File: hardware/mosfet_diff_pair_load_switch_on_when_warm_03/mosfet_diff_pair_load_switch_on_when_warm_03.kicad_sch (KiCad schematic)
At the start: 18 parts, among them Q1 IRLML2402TR, Q2 IRLML2402TR

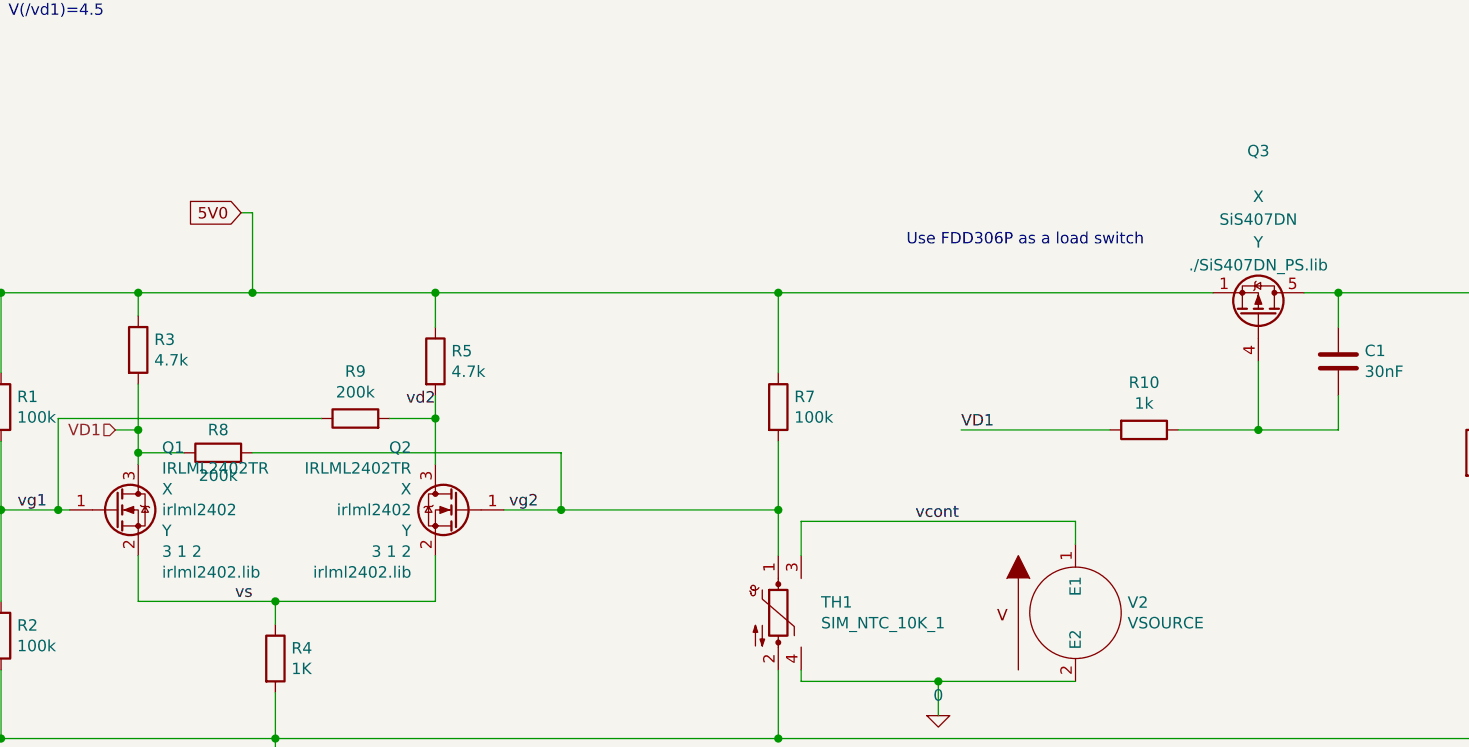
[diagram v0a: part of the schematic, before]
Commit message: Changing pass transistor from FDD306 and long-tail pair transistors from irlml2402 becuase they aren't available at the moment.
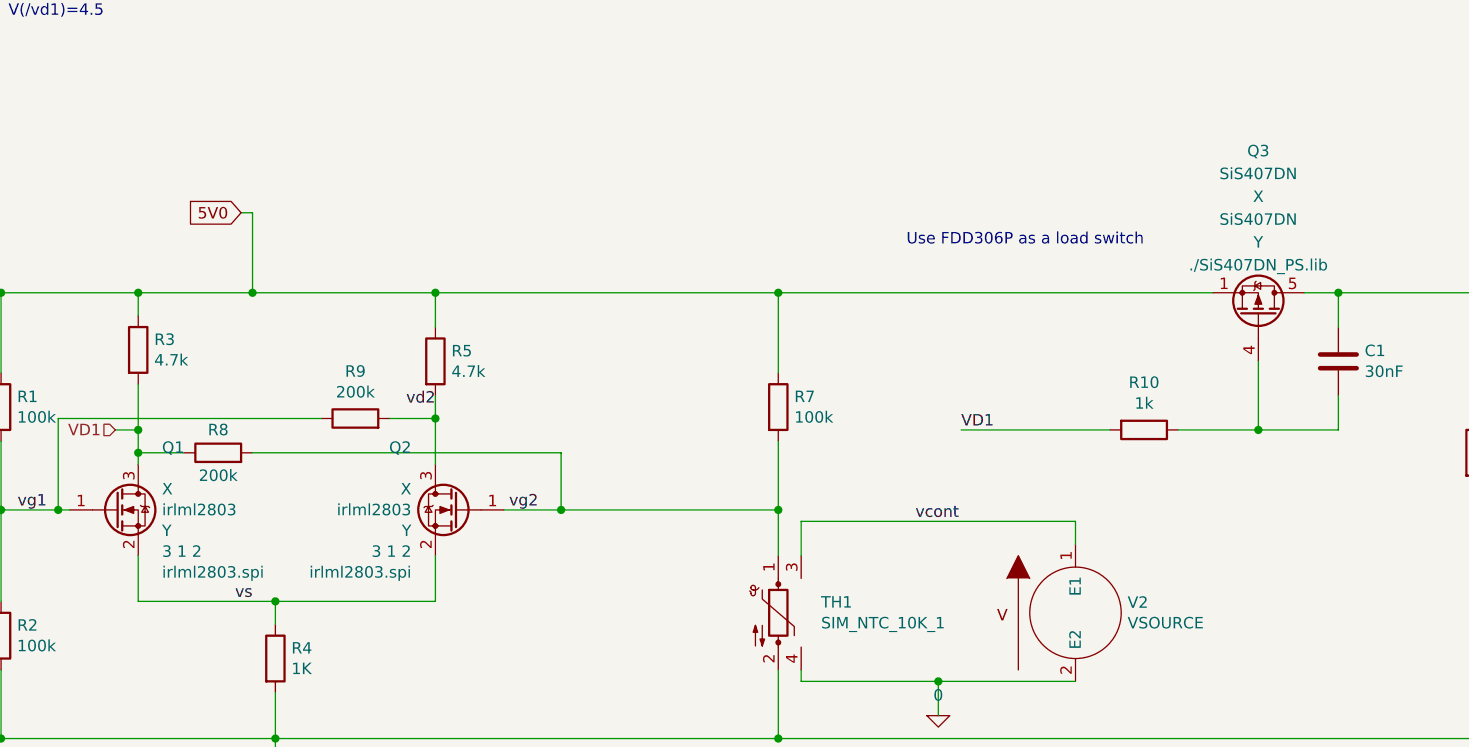
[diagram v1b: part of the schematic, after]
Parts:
- Q1, Q2: value IRLML2402TR -> (none); footprint Package_TO_SOT_SMD:SOT-23 -> (none); Spice_Lib_File irlml2402.lib -> irlml2803.spi; Spice_Model irlml2402 -> irlml2803
- Q3: value (none) -> SiS407DN; footprint (none) -> Package_SO:Vishay_PowerPAK_1212-8_Single
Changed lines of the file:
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@@
       (effects (font (size 1.27 1.27)) (justify left))
     )
-    (property "Value" "IRLML2402TR" (id 1) (at 102.9716 93.1672 0)
+    (property "Value" "" (id 1) (at 102.9716 93.1672 0)
       (effects (font (size 1.27 1.27)) (justify left))
     )
-    (property "Footprint" "Package_TO_SOT_SMD:SOT-23" (id 2) (at 102.87 99.695 0)
+    (property "Footprint" "" (id 2) (at 102.87 99.695 0)
       (effects (font (size 1.27 1.27) italic) (justify left) hide)
     )
@@
       (effects (font (size 1.27 1.27)) (justify left))
     )
-    (property "Spice_Model" "irlml2402" (id 5) (at 102.9716 97.79 0)
+    (property "Spice_Model" "irlml2803" (id 5) (at 102.9716 97.79 0)
       (effects (font (size 1.27 1.27)) (justify left))
     )
@@
       (effects (font (size 1.27 1.27)) (justify left))
     )
-    (property "Spice_Lib_File" "irlml2402.lib" (id 8) (at 102.9716 104.7242 0)
+    (property "Spice_Lib_File" "irlml2803.spi" (id 8) (at 102.9716 104.7242 0)
       (effects (font (size 1.27 1.27)) (justify left))
     )
@@
       (effects (font (size 1.27 1.27)) (justify left))
     )
-    (property "Value" "IRLML2402TR" (id 1) (at 130.683 93.1672 0)
+    (property "Value" "" (id 1) (at 130.683 93.1672 0)
       (effects (font (size 1.27 1.27)) (justify left))
     )
-    (property "Footprint" "Package_TO_SOT_SMD:SOT-23" (id 2) (at 130.81 99.695 0)
+    (property "Footprint" "" (id 2) (at 130.81 99.695 0)
       (effects (font (size 1.27 1.27) italic) (justify left) hide)
     )
@@
       (effects (font (size 1.27 1.27)) (justify left))
     )
-    (property "Spice_Model" "irlml2402" (id 5) (at 130.683 97.79 0)
+    (property "Spice_Model" "irlml2803" (id 5) (at 130.683 97.79 0)
       (effects (font (size 1.27 1.27)) (justify left))
     )
@@
       (effects (font (size 1.27 1.27)) (justify left))
     )
-    (property "Spice_Lib_File" "irlml2402.lib" (id 8) (at 130.683 104.7242 0)
+    (property "Spice_Lib_File" "irlml2803.spi" (id 8) (at 130.683 104.7242 0)
       (effects (font (size 1.27 1.27)) (justify left))
     )
@@
     (in_bom yes) (on_board yes) (fields_autoplaced)
     (property "Reference" "Q3" (id 0) (at 224.79 57.9076 90))
-    (property "Value" "" (id 1) (at 224.79 60.4445 90))
-    (property "Footprint" "" (id 2) (at 222.885 71.12 0)
+    (property "Value" "SiS407DN" (id 1) (at 224.79 60.4445 90))
+    (property "Footprint" "Package_SO:Vishay_PowerPAK_1212-8_Single" (id 2) (at 222.885 71.12 0)
       (effects (font (size 1.27 1.27) italic) (justify left) hide)
     )
@@
     )
     (path "/00000000-0000-0000-0000-000060a27f5b"
-      (reference "Q1") (unit 1) (value "IRLML2402TR") (footprint "Package_TO_SOT_SMD:SOT-23")
+      (reference "Q1") (unit 1) (value "irlml2803") (footprint "Package_TO_SOT_SMD:SOT-23")
     )
     (path "/00000000-0000-0000-0000-000060a2fa09"
-      (reference "Q2") (unit 1) (value "IRLML2402TR") (footprint "Package_TO_SOT_SMD:SOT-23")
+      (reference "Q2") (unit 1) (value "irlml2803") (footprint "Package_TO_SOT_SMD:SOT-23")
     )
     (path "/ffcdfa39-bc4e-49d0-acb0-8b5d14b3a0df"
